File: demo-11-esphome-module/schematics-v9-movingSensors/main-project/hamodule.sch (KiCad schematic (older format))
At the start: 55 parts, among them J1 1017505, J2 Conn-ESP-Relays, J3 1017505, J4 Conn-Buttons, J5 Conn_01x02, J6 Conn-Esp-Sensors, J7 Conn-LedIndicators, J8 1017505, K1 G5Q-1, K2 G5Q-1, K3 G5Q-1, K4 G5Q-1, U1 ULN2003A, U2 LD1117S33TR_SOT223, U3 HCPL3700, U4 HCPL3700, U5 HCPL3700, U6 HCPL3700

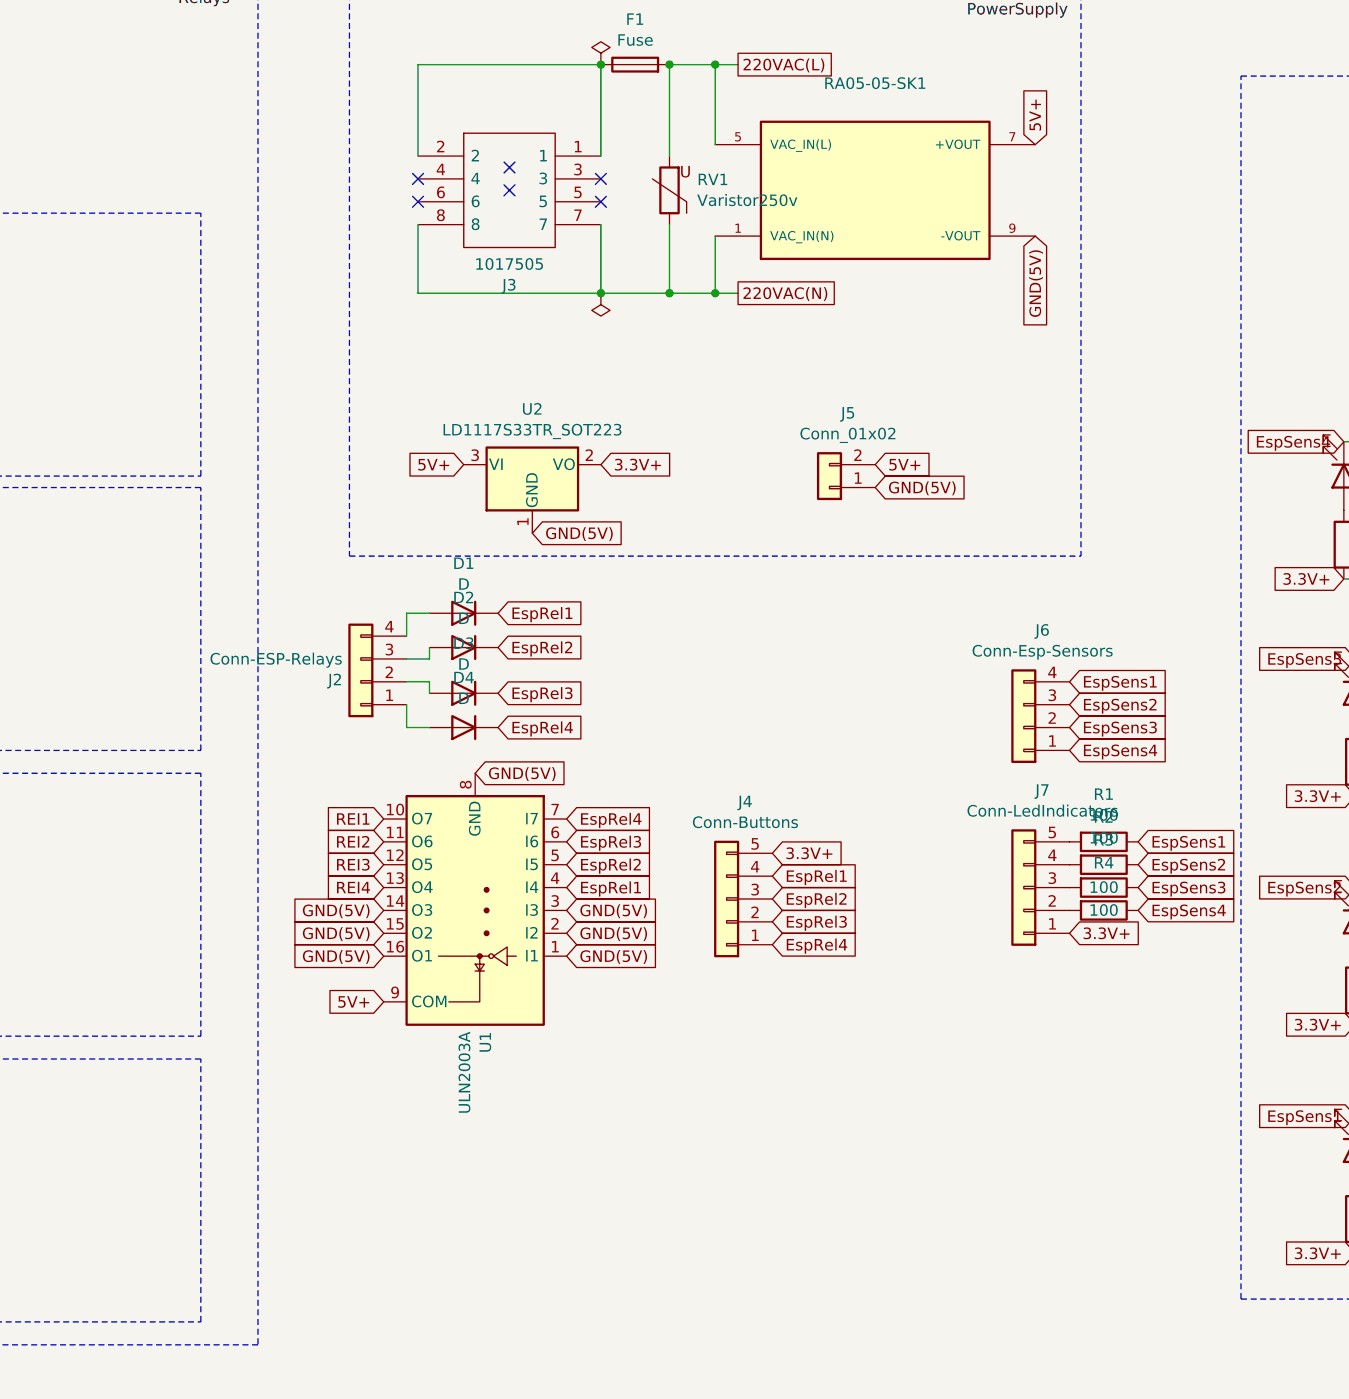
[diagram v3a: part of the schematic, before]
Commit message: adding caps
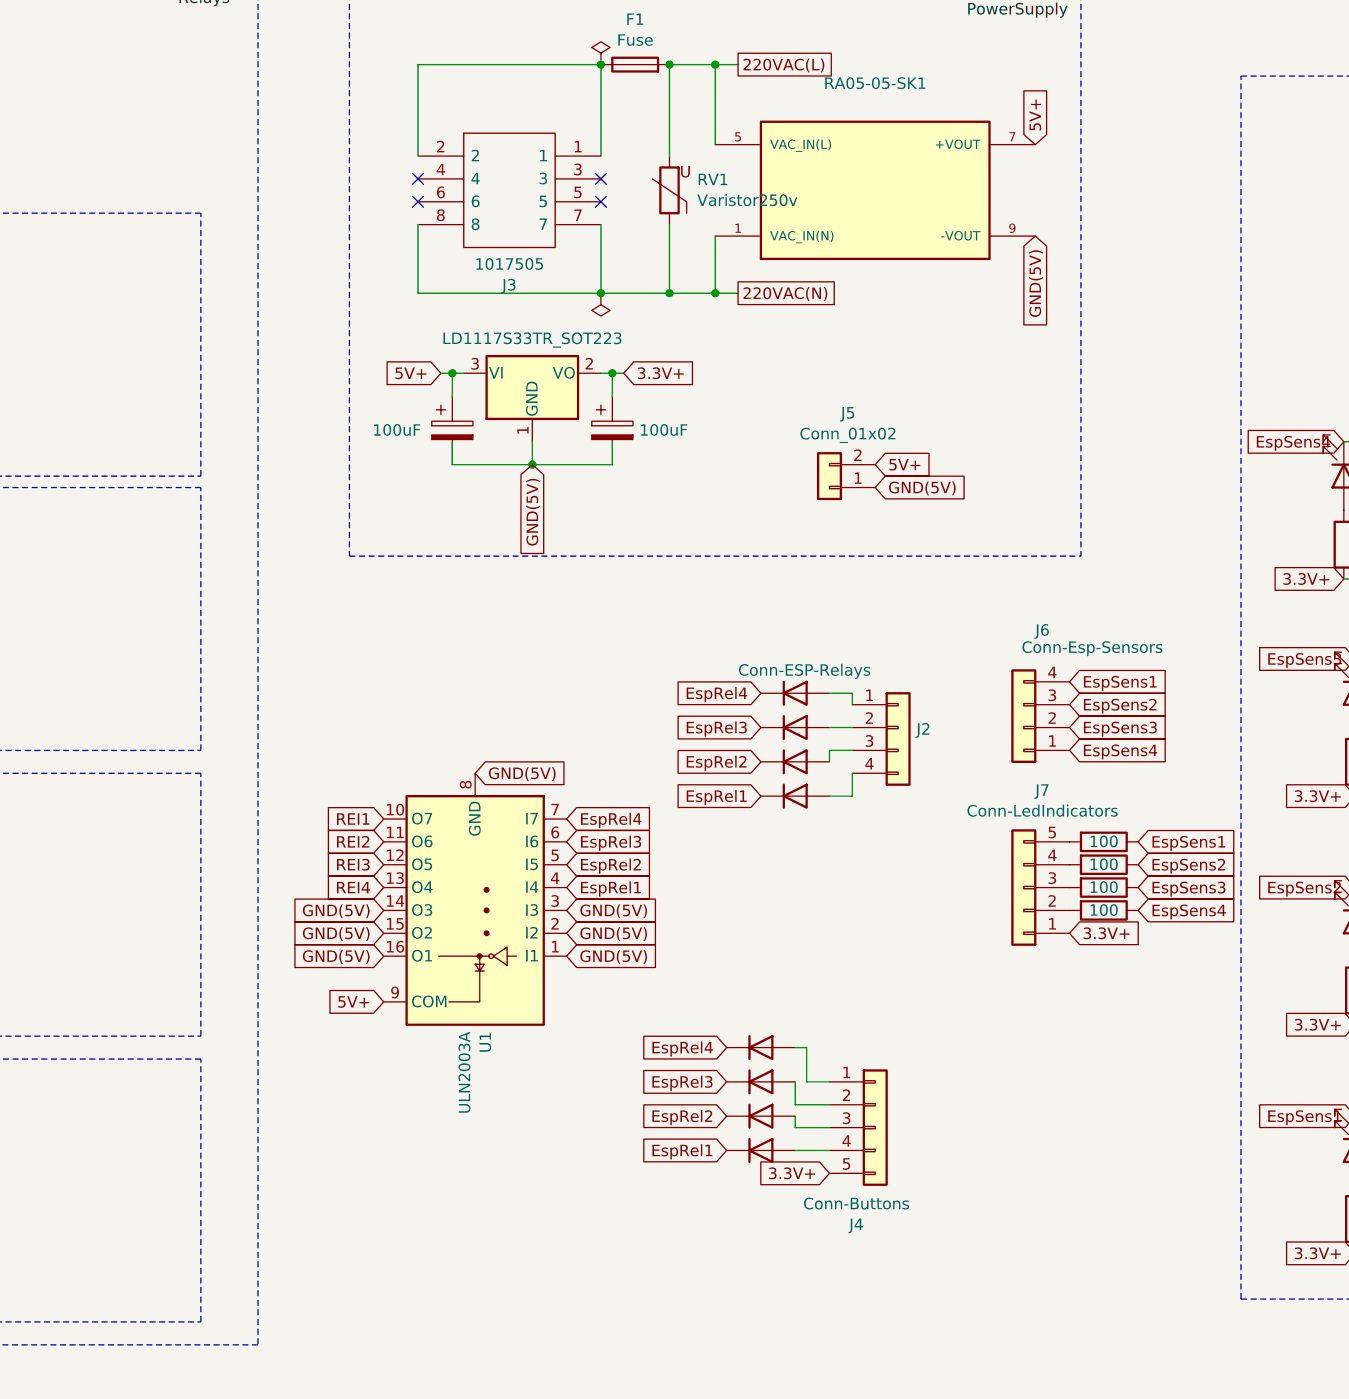
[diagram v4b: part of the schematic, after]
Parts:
- added C1, C2: 100uF, Capacitor_THT:CP_Radial_D6.3mm_P2.50mm, symbol Device:CP
- added D10, D11, D12, D9: D, Diode_THT:D_A-405_P7.62mm_Horizontal, symbol Device:D
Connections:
- net 3.3V+: now also C2.1
- net 5V+: now also C1.1
- net EspRel1: now also D12.1 (K); no longer J4.4 (Pin_4)
- net EspRel2: now also D11.1 (K); no longer J4.3 (Pin_3)
- net EspRel3: now also D10.1 (K); no longer J4.2 (Pin_2)
- net EspRel4: now also D9.1 (K); no longer J4.1 (Pin_1)
- net GND(5V): now also C1.2, C2.2
- new net: D12.2 (A), J4.4 (Pin_4)
- new net: D11.2 (A), J4.3 (Pin_3)
- new net: D9.2 (A), J4.1 (Pin_1)
- new net: D10.2 (A), J4.2 (Pin_2)
- no-connect marks 22 -> 20
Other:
- moved on the sheet: J2, J4

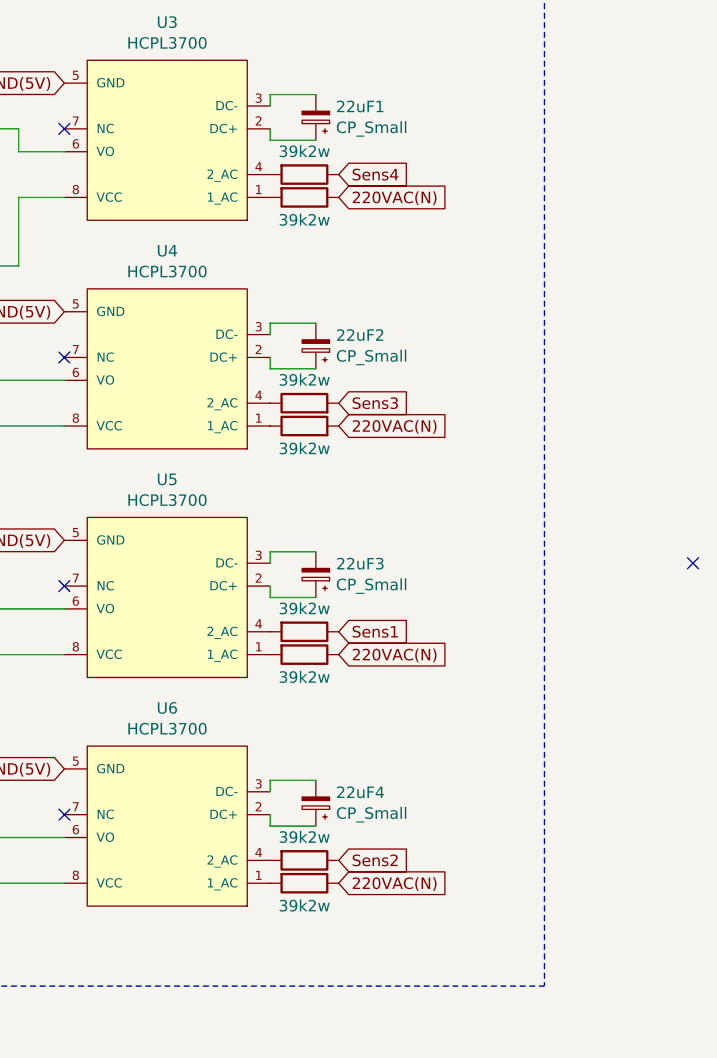
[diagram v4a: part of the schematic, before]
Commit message: caps are wrong way around
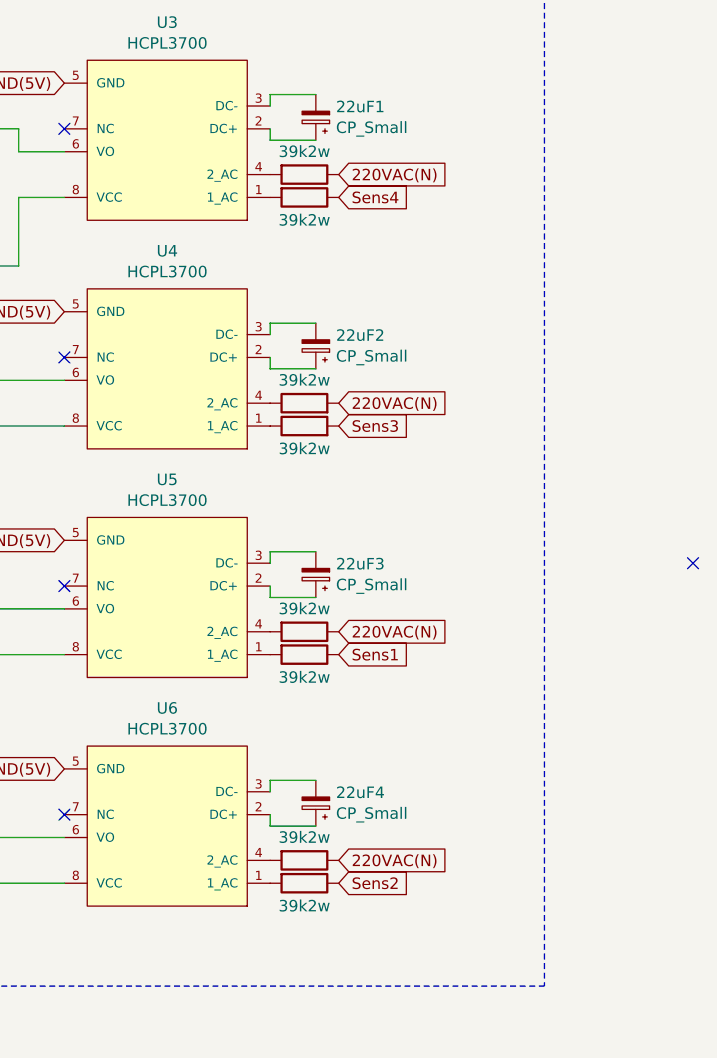
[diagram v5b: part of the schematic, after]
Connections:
- net at R13.2: now also U5.1 (1_AC); no longer U5.4 (2_AC)
- net at R14.2: now also U5.4 (2_AC); no longer U5.1 (1_AC)
- net at U3.1 (1_AC): now also R9.2; no longer R10.2
- net at U3.4 (2_AC): now also R10.2; no longer R9.2
- net at R16.2: now also U6.4 (2_AC); no longer U6.1 (1_AC)
- net at R15.2: now also U6.1 (1_AC); no longer U6.4 (2_AC)
- net at U4.1 (1_AC): now also R11.1; no longer R12.1
- net at U4.4 (2_AC): now also R12.1; no longer R11.1
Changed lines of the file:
@@
 	1    0    0    -1
 $EndComp
-Text GLabel 10100 5750 2    50   Input ~ 0
+Text GLabel 10100 5850 2    50   Input ~ 0
 Sens2
-Text GLabel 10100 3750 2    50   Input ~ 0
-Sens3
-Text GLabel 10100 2750 2    50   Input ~ 0
+Text GLabel 10100 2850 2    50   Input ~ 0
 Sens4
 $Comp
 L Device:R R14
 U 1 1 61354B0C
-P 9950 4850
-F 0 "R14" V 9743 4850 50  0001 C CNN
-F 1 "39k2w" V 10050 4850 50  0000 C CNN
-F 2 "Resistor_THT:R_Axial_DIN0516_L15.5mm_D5.0mm_P20.32mm_Horizontal" V 9880 4850 50  0001 C CNN
-F 3 "~" H 9950 4850 50  0001 C CNN
-	1    9950 4850
-	0    1    1    0
-$EndComp
-Text GLabel 10100 4750 2    50   Input ~ 0
+P 9950 4750
+F 0 "R14" V 9743 4750 50  0001 C CNN
+F 1 "39k2w" V 9850 4750 50  0000 C CNN
+F 2 "Resistor_THT:R_Axial_DIN0516_L15.5mm_D5.0mm_P20.32mm_Horizontal" V 9880 4750 50  0001 C CNN
+F 3 "~" H 9950 4750 50  0001 C CNN
+	1    9950 4750
+	0    1    1    0
+$EndComp
+Text GLabel 10100 4850 2    50   Input ~ 0
 Sens1
 $Comp
@@
 Text GLabel 8900 3350 0    50   Input ~ 0
 GND(5V)
-Text GLabel 10100 5850 2    50   Input ~ 0
+Text GLabel 10100 5750 2    50   Input ~ 0
 220VAC(N)
 $Comp
 L Device:R R16
 U 1 1 613B1E37
+P 9950 5750
+F 0 "R16" V 9743 5750 50  0001 C CNN
+F 1 "39k2w" V 9850 5750 50  0000 C CNN
+F 2 "Resistor_THT:R_Axial_DIN0516_L15.5mm_D5.0mm_P20.32mm_Horizontal" V 9880 5750 50  0001 C CNN
+F 3 "~" H 9950 5750 50  0001 C CNN
+	1    9950 5750
+	0    1    1    0
+$EndComp
+$Comp
+L Device:R R15
+U 1 1 613B1E3D
 P 9950 5850
-F 0 "R16" V 9743 5850 50  0001 C CNN
+F 0 "R15" V 9743 5850 50  0001 C CNN
 F 1 "39k2w" V 10050 5850 50  0000 C CNN
 F 2 "Resistor_THT:R_Axial_DIN0516_L15.5mm_D5.0mm_P20.32mm_Horizontal" V 9880 5850 50  0001 C CNN
 F 3 "~" H 9950 5850 50  0001 C CNN
 	1    9950 5850
-	0    1    1    0
-$EndComp
-$Comp
-L Device:R R15
-U 1 1 613B1E3D
-P 9950 5750
-F 0 "R15" V 9743 5750 50  0001 C CNN
-F 1 "39k2w" V 9850 5750 50  0000 C CNN
-F 2 "Resistor_THT:R_Axial_DIN0516_L15.5mm_D5.0mm_P20.32mm_Horizontal" V 9880 5750 50  0001 C CNN
-F 3 "~" H 9950 5750 50  0001 C CNN
-	1    9950 5750
 	0    1    1    0
 $EndComp
@@
 Text GLabel 8900 4350 0    50   Input ~ 0
 GND(5V)
-Text GLabel 10100 3850 2    50   Input ~ 0
-220VAC(N)
-$Comp
-L Device:R R11
-U 1 1 613B6B92
-P 9950 3750
-F 0 "R11" V 9743 3750 50  0001 C CNN
-F 1 "39k2w" V 10050 3750 50  0000 C CNN
-F 2 "Resistor_THT:R_Axial_DIN0516_L15.5mm_D5.0mm_P20.32mm_Horizontal" V 9880 3750 50  0001 C CNN
-F 3 "~" H 9950 3750 50  0001 C CNN
-	1    9950 3750
-	0    -1   -1   0
-$EndComp
-$Comp
-L Device:R R12
-U 1 1 613B6B98
-P 9950 3850
-F 0 "R12" V 9743 3850 50  0001 C CNN
-F 1 "39k2w" V 9850 3850 50  0000 C CNN
-F 2 "Resistor_THT:R_Axial_DIN0516_L15.5mm_D5.0mm_P20.32mm_Horizontal" V 9880 3850 50  0001 C CNN
-F 3 "~" H 9950 3850 50  0001 C CNN
-	1    9950 3850
-	0    -1   -1   0
-$EndComp
 $Comp
 L HCPL-3700-000:HCPL3700 U5
@@
 Text GLabel 8900 5350 0    50   Input ~ 0
 GND(5V)
-Text GLabel 10100 2850 2    50   Input ~ 0
+Text GLabel 10100 2750 2    50   Input ~ 0
 220VAC(N)
 $Comp
 L Device:R R10
 U 1 1 613BAE41
+P 9950 2750
+F 0 "R10" V 9743 2750 50  0001 C CNN
+F 1 "39k2w" V 9850 2750 50  0000 C CNN
+F 2 "Resistor_THT:R_Axial_DIN0516_L15.5mm_D5.0mm_P20.32mm_Horizontal" V 9880 2750 50  0001 C CNN
+F 3 "~" H 9950 2750 50  0001 C CNN
+	1    9950 2750
+	0    1    1    0
+$EndComp
+$Comp
+L Device:R R9
+U 1 1 613BAE47
 P 9950 2850
-F 0 "R10" V 9743 2850 50  0001 C CNN
+F 0 "R9" V 9743 2850 50  0001 C CNN
 F 1 "39k2w" V 10050 2850 50  0000 C CNN
 F 2 "Resistor_THT:R_Axial_DIN0516_L15.5mm_D5.0mm_P20.32mm_Horizontal" V 9880 2850 50  0001 C CNN
 F 3 "~" H 9950 2850 50  0001 C CNN
 	1    9950 2850
-	0    1    1    0
-$EndComp
-$Comp
-L Device:R R9
-U 1 1 613BAE47
-P 9950 2750
-F 0 "R9" V 9743 2750 50  0001 C CNN
-F 1 "39k2w" V 9850 2750 50  0000 C CNN
-F 2 "Resistor_THT:R_Axial_DIN0516_L15.5mm_D5.0mm_P20.32mm_Horizontal" V 9880 2750 50  0001 C CNN
-F 3 "~" H 9950 2750 50  0001 C CNN
-	1    9950 2750
 	0    1    1    0
 $EndComp
@@
 	0    1    1    0
 $EndComp
-Text GLabel 10100 4850 2    50   Input ~ 0
+Text GLabel 10100 4750 2    50   Input ~ 0
 220VAC(N)
 $Comp
 L Device:R R13
 U 1 1 61314DEF
-P 9950 4750
-F 0 "R13" V 9743 4750 50  0001 C CNN
-F 1 "39k2w" V 9850 4750 50  0000 C CNN
-F 2 "Resistor_THT:R_Axial_DIN0516_L15.5mm_D5.0mm_P20.32mm_Horizontal" V 9880 4750 50  0001 C CNN
-F 3 "~" H 9950 4750 50  0001 C CNN
-	1    9950 4750
+P 9950 4850
+F 0 "R13" V 9743 4850 50  0001 C CNN
+F 1 "39k2w" V 10050 4850 50  0000 C CNN
+F 2 "Resistor_THT:R_Axial_DIN0516_L15.5mm_D5.0mm_P20.32mm_Horizontal" V 9880 4850 50  0001 C CNN
+F 3 "~" H 9950 4850 50  0001 C CNN
+	1    9950 4850
 	0    1    1    0
 $EndComp
@@
 Wire Wire Line
 	4250 2250 4300 2250
+$Comp
+L Device:R R12
+U 1 1 613B6B98
+P 9950 3750
+F 0 "R12" V 9743 3750 50  0001 C CNN
+F 1 "39k2w" V 10050 3750 50  0000 C CNN
+F 2 "Resistor_THT:R_Axial_DIN0516_L15.5mm_D5.0mm_P20.32mm_Horizontal" V 9880 3750 50  0001 C CNN
+F 3 "~" H 9950 3750 50  0001 C CNN
+	1    9950 3750
+	0    -1   -1   0
+$EndComp
+$Comp
+L Device:R R11
+U 1 1 613B6B92
+P 9950 3850
+F 0 "R11" V 9743 3850 50  0001 C CNN
+F 1 "39k2w" V 9850 3850 50  0000 C CNN
+F 2 "Resistor_THT:R_Axial_DIN0516_L15.5mm_D5.0mm_P20.32mm_Horizontal" V 9880 3850 50  0001 C CNN
+F 3 "~" H 9950 3850 50  0001 C CNN
+	1    9950 3850
+	0    -1   -1   0
+$EndComp
+Text GLabel 10100 3750 2    50   Input ~ 0
+220VAC(N)
+Text GLabel 10100 3850 2    50   Input ~ 0
+Sens3
 $EndSCHEMATC

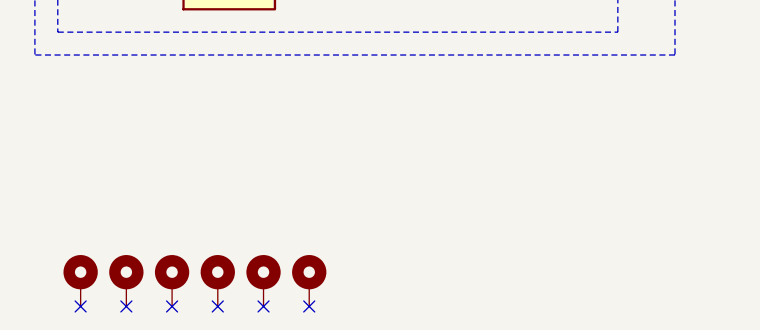
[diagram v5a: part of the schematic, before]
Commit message: adding mounting holes for ESP board
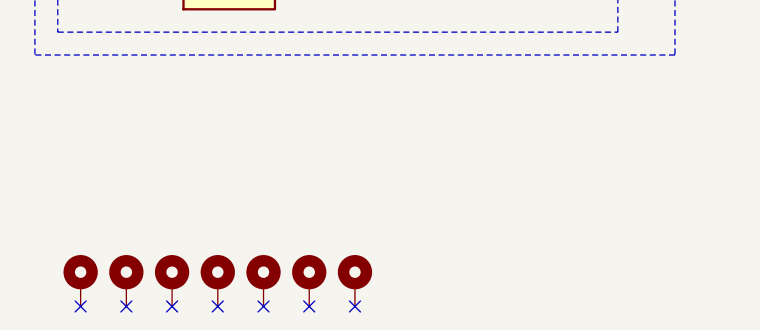
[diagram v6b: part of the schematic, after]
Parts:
- added H7: MountingHole_Pad, MountingHole:MountingHole_3.2mm_M3_ISO14580_Pad, symbol Mechanical:MountingHole_Pad
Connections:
- no-connect marks 20 -> 21
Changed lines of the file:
@@
 Text GLabel 10100 3850 2    50   Input ~ 0
 Sens3
+$Comp
+L Mechanical:MountingHole_Pad H7
+U 1 1 615876D7
+P 2000 7500
+F 0 "H7" H 2100 7549 50  0001 L CNN
+F 1 "MountingHole_Pad" H 2100 7458 50  0001 L CNN
+F 2 "MountingHole:MountingHole_3.2mm_M3_ISO14580_Pad" H 2000 7500 50  0001 C CNN
+F 3 "~" H 2000 7500 50  0001 C CNN
+	1    2000 7500
+	1    0    0    -1
+$EndComp
+NoConn ~ 2000 7600
 $EndSCHEMATC

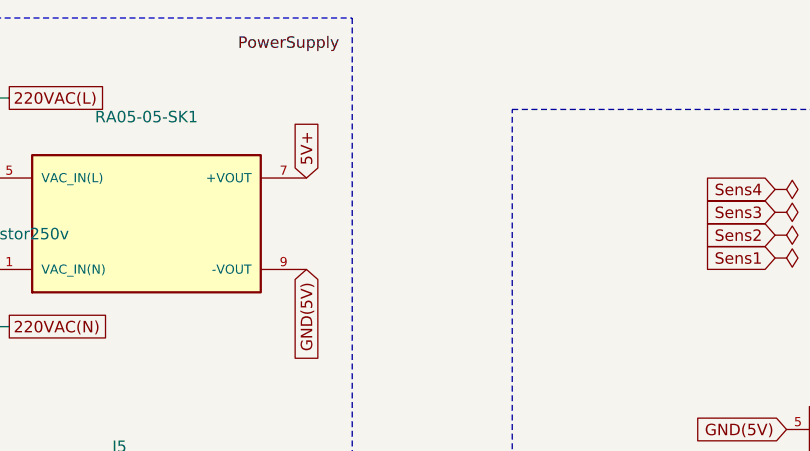
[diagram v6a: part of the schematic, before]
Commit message: adding pins to mesure current
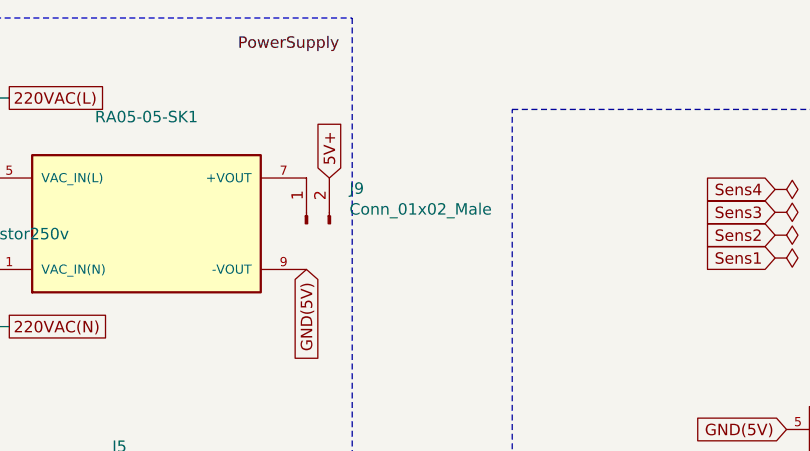
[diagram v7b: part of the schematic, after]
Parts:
- added J9: Conn_01x02_Male, Connector_PinHeader_2.54mm:PinHeader_1x02_P2.54mm_Vertical, symbol Connector:Conn_01x02_Male
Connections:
- net 5V+: now also J9.2 (Pin_2); no longer RA05-05-SK1.7 (+VOUT)
- new net: J9.1 (Pin_1), RA05-05-SK1.7 (+VOUT)
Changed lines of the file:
@@
 Text GLabel 6800 1650 3    50   Input ~ 0
 GND(5V)
-Text GLabel 6800 1250 1    50   Input ~ 0
+Text GLabel 6900 1250 1    50   Input ~ 0
 5V+
 Text GLabel 5500 1900 2    50   UnSpc ~ 0
@@
 $EndComp
 NoConn ~ 2000 7600
+$Comp
+L Connector:Conn_01x02_Male J9
+U 1 1 6159F81D
+P 6800 1450
+F 0 "J9" V 6954 1262 50  0000 R CNN
+F 1 "Conn_01x02_Male" V 6863 1262 50  0000 R CNN
+F 2 "Connector_PinHeader_2.54mm:PinHeader_1x02_P2.54mm_Vertical" H 6800 1450 50  0001 C CNN
+F 3 "~" H 6800 1450 50  0001 C CNN
+	1    6800 1450
+	0    -1   -1   0
+$EndComp
 $EndSCHEMATC
